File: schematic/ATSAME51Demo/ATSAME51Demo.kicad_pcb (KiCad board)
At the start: 4 copper layers, 0 parts

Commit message: First draft PCB layout
Still needs silkscreen cleanup
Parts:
- added C1: 100n, Capacitor_SMD:C_0402_1005Metric, F.Cu at (109.7, 120.5)
- added C10: 100n, Capacitor_SMD:C_0402_1005Metric, F.Cu at (90.8, 109.3)
- added C11: 4.7uF, Capacitor_SMD:C_0603_1608Metric, F.Cu at (101.7, 97.2)
- added C12: 100n, Capacitor_SMD:C_0402_1005Metric, F.Cu at (103.0, 97.5)
- added C14: 100n, Capacitor_SMD:C_0603_1608Metric, F.Cu at (64.7, 138.1)
- added C15: 10uF, Capacitor_SMD:C_0603_1608Metric, F.Cu at (64.7, 141.0)
- added C16: 100n, Capacitor_SMD:C_0603_1608Metric, F.Cu at (74.6, 73.1)
- added C17: 220n, Capacitor_SMD:C_0603_1608Metric, F.Cu at (64.1, 65.8)
- added C2: 20p, Capacitor_SMD:C_0603_1608Metric, F.Cu at (88.5, 102.9)
- added C3: 20p, Capacitor_SMD:C_0603_1608Metric, F.Cu at (88.5, 104.5)
- added C4: 100n, Capacitor_SMD:C_0402_1005Metric, F.Cu at (98.5, 118.3)
- added C5: 100n, Capacitor_SMD:C_0402_1005Metric, F.Cu at (107.8, 114.0)
- added C6: 100n, Capacitor_SMD:C_0402_1005Metric, F.Cu at (107.6, 106.0)
- added C7: 10uF, Capacitor_SMD:C_0805_2012Metric, F.Cu at (137.2, 142.0)
- added C8: 100n, Capacitor_SMD:C_0402_1005Metric, F.Cu at (100.3, 101.7)
- added C9: 22uF, Capacitor_SMD:C_0603_1608Metric, F.Cu at (138.8, 137.6)
- added D1: Red, LED_SMD:LED_0603_1608Metric, F.Cu at (127.9, 155.8)
- added D2: Red, LED_SMD:LED_0603_1608Metric, F.Cu at (56.9, 111.8)
- added D3: MBR0520LT, Diode_SMD:D_SOD-123, F.Cu at (145.3, 85.8)
- added D4: MBR0520LT, Diode_SMD:D_SOD-123, F.Cu at (57.6, 79.0)
- added D5: Yellow, LED_SMD:LED_0603_1608Metric, F.Cu at (61.4, 111.8)
- added D6: Blue, LED_SMD:LED_0603_1608Metric, F.Cu at (120.4, 75.5)
- added D7: Green, LED_SMD:LED_0603_1608Metric, F.Cu at (124.9, 75.5)
- added D8: Green, LED_SMD:LED_0603_1608Metric, F.Cu at (80.5, 70.7)
- added D9: Yellow, LED_SMD:LED_0603_1608Metric, F.Cu at (80.5, 67.0)
- added IC1: ATSAME51J20A-AU, SamacSys_Parts:QFP50P1200X1200X120-64N, F.Cu at (100.0, 110.0)
- added IC2: AZ1117IH-3.3TRG1, SamacSys_Parts:SOT230P700X180-4N, F.Cu at (144.2, 138.9)
- added IC3: MCP2221-I_SL, SamacSys_Parts:SOIC127P600X175-14N, F.Cu at (69.5, 67.1)
- added J1: Barrel_Jack_Switch, Connector_BarrelJack:BarrelJack_Wuerth_6941xx301002, F.Cu at (142.4, 145.3)
- added J10: Conn_02x06_Odd_Even, Connector_PinHeader_2.54mm:PinHeader_2x06_P2.54mm_Vertical, F.Cu at (79.5, 156.8)
- added J11: Conn_02x07_Odd_Even, Connector_PinHeader_2.54mm:PinHeader_2x07_P2.54mm_Vertical, F.Cu at (71.0, 103.0)
- added J12: Conn_01x02, Connector_PinHeader_2.54mm:PinHeader_1x02_P2.54mm_Vertical, F.Cu at (101.4, 70.3)
- added J13: Conn_01x08, Connector_PinHeader_2.54mm:PinHeader_1x08_P2.54mm_Horizontal, F.Cu at (94.0, 65.0)
- added J14: Conn_02x08_Odd_Even, Connector_PinHeader_2.54mm:PinHeader_2x08_P2.54mm_Vertical, F.Cu at (89.3, 138.0)
- added J15: Conn_02x06_Odd_Even, Connector_PinHeader_2.54mm:PinHeader_2x06_P2.54mm_Vertical, F.Cu at (132.0, 117.0)
- added J16: Conn_02x07_Odd_Even, Connector_PinHeader_2.54mm:PinHeader_2x07_P2.54mm_Vertical, F.Cu at (109.4, 80.2)
- added J2: Power, Connector_PinHeader_2.54mm:PinHeader_2x03_P2.54mm_Vertical, F.Cu at (128.3, 146.5)
- added J3: Conn_01x02, Connector_PinHeader_2.54mm:PinHeader_1x02_P2.54mm_Vertical, F.Cu at (58.1, 120.5)
- added J4: USB_B_Micro, Connector_USB:USB_Micro-B_Amphenol_10104110_Horizontal, F.Cu at (147.2, 77.2)
- added J5: USB_B_Mini, Connector_USB:USB_Mini-B_Wuerth_65100516121_Horizontal, F.Cu at (55.4, 69.5)
- added J6: Conn_01x02, Connector_PinHeader_2.54mm:PinHeader_1x02_P2.54mm_Vertical, F.Cu at (121.4, 84.4)
- added J7: Conn_02x02_Odd_Even, Connector_PinHeader_2.54mm:PinHeader_2x02_P2.54mm_Vertical, F.Cu at (129.5, 123.2)
- added J8: Conn_02x02_Odd_Even, Connector_PinHeader_2.54mm:PinHeader_2x02_P2.54mm_Vertical, F.Cu at (129.2, 135.3)
- added J9: Micro SD Card, SamacSys_Parts:MEM20750014001A, F.Cu at (65.0, 154.0)
- added L1: 470R, Inductor_SMD:L_0603_1608Metric, F.Cu at (88.2, 109.5)
- added L2: 10uH, Inductor_SMD:L_0603_1608Metric, F.Cu at (101.6, 100.3)
- added R1: 100k, Resistor_SMD:R_0603_1608Metric, F.Cu at (132.1, 63.6)
- added R10: 100k, Resistor_SMD:R_0603_1608Metric, F.Cu at (84.1, 149.9)
- added R11: 4k7, Resistor_SMD:R_0603_1608Metric, F.Cu at (128.7, 129.2)
- added R12: 100k, Resistor_SMD:R_0603_1608Metric, F.Cu at (87.5, 149.9)
- added R13: 10k, Resistor_SMD:R_0603_1608Metric, F.Cu at (90.8, 149.9)
- added R14: 4k7, Resistor_SMD:R_0603_1608Metric, F.Cu at (132.3, 129.4)
- added R15: 100k, Resistor_SMD:R_0603_1608Metric, F.Cu at (80.8, 149.9)
- added R16: 10k, Resistor_SMD:R_0603_1608Metric, F.Cu at (94.2, 149.9)
- added R17: 10k, Resistor_SMD:R_0603_1608Metric, F.Cu at (105.1, 70.0)
- added R18: 10k, Resistor_SMD:R_0603_1608Metric, F.Cu at (78.7, 63.5)
- added R19: 220R, Resistor_SMD:R_0603_1608Metric, F.Cu at (77.4, 70.7)
- added R2: 220R, Resistor_SMD:R_0603_1608Metric, F.Cu at (132.3, 155.8)
- added R20: 220R, Resistor_SMD:R_0603_1608Metric, F.Cu at (77.4, 67.0)
- added R5: 220R, Resistor_SMD:R_0603_1608Metric, F.Cu at (56.9, 115.4)
- added R6: 220R, Resistor_SMD:R_0603_1608Metric, F.Cu at (61.4, 115.4)
- added R7: 220R, Resistor_SMD:R_0603_1608Metric, F.Cu at (120.4, 79.6)
- added R8: 220R, Resistor_SMD:R_0603_1608Metric, F.Cu at (124.9, 79.6)
- added R9: 100k, Resistor_SMD:R_0603_1608Metric, F.Cu at (77.4, 149.9)
- added SW1: SW_MEC_5E, SamacSys_Parts:PTS647SK38SMTR2LFS, F.Cu at (125.0, 65.4)
- added SW2: SW_MEC_5E, SamacSys_Parts:FSM16JH, F.Cu at (60.5, 91.8)
- added SW3: SW_MEC_5E, SamacSys_Parts:FSM16JH, F.Cu at (80.8, 91.8)
- added X1: 12 MHz, SamacSys_Parts:ASTMUPCE3312000MHZLJET, F.Cu at (107.1, 120.5)
- added X2: 32.768 kHz 12.5 pF, SamacSys_Parts:CM9VT1A, F.Cu at (91.1, 103.7)
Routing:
- net VIN: track 0.00 -> 170.9 mm, vias 0 -> 2
- net SD_CD: track 0.00 -> 94.4 mm, vias 0 -> 1
- net GND: track 0.00 -> 88.5 mm, vias 0 -> 29
- net TX0: track 0.00 -> 78.5 mm, vias 0 -> 1
- net RX0: track 0.00 -> 78.0 mm, vias 0 -> 2
- net SD_CLK: track 0.00 -> 71.3 mm, vias 0 -> 1
- net SD_DAT0: track 0.00 -> 71.0 mm, vias 0 -> 2
- net SD_DAT1: track 0.00 -> 69.6 mm, vias 0 -> 2
- net SD_CMD: track 0.00 -> 66.0 mm, vias 0 -> 2
- net SD_DAT3: track 0.00 -> 64.3 mm, vias 0 -> 2
- net RESETN: track 0.00 -> 64.2 mm, vias 0 -> 2
- net SD_DAT2: track 0.00 -> 61.0 mm, vias 0 -> 2
- net VCC3V3: track 0.00 -> 57.0 mm, vias 0 -> 15
- net PB04: track 0.00 -> 54.0 mm
- net PB31: track 0.00 -> 53.6 mm, vias 0 -> 1
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- added copper zone on In1.Cu, net GND
- added copper zone on In2.Cu, net VCC3V3
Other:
- board outline added: 100 x 100 mm

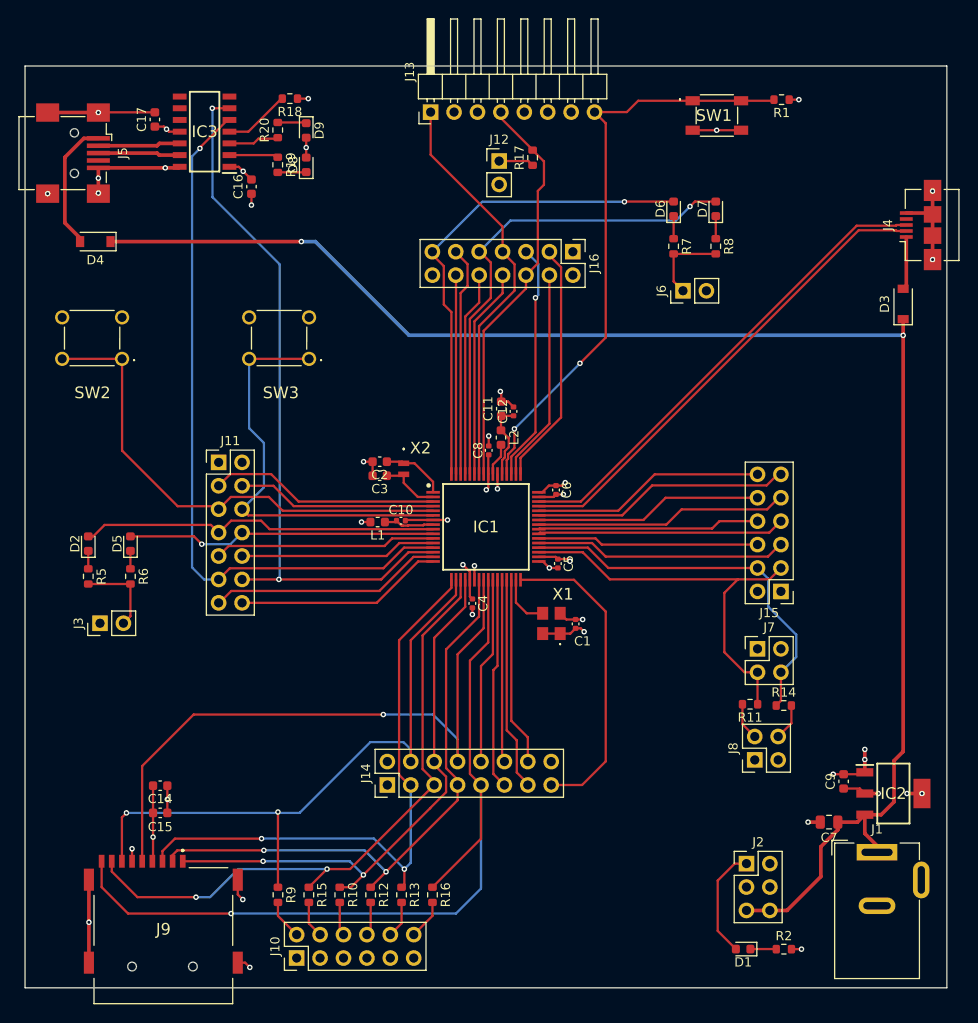
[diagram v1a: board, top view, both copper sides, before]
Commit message: Front silkscreen done
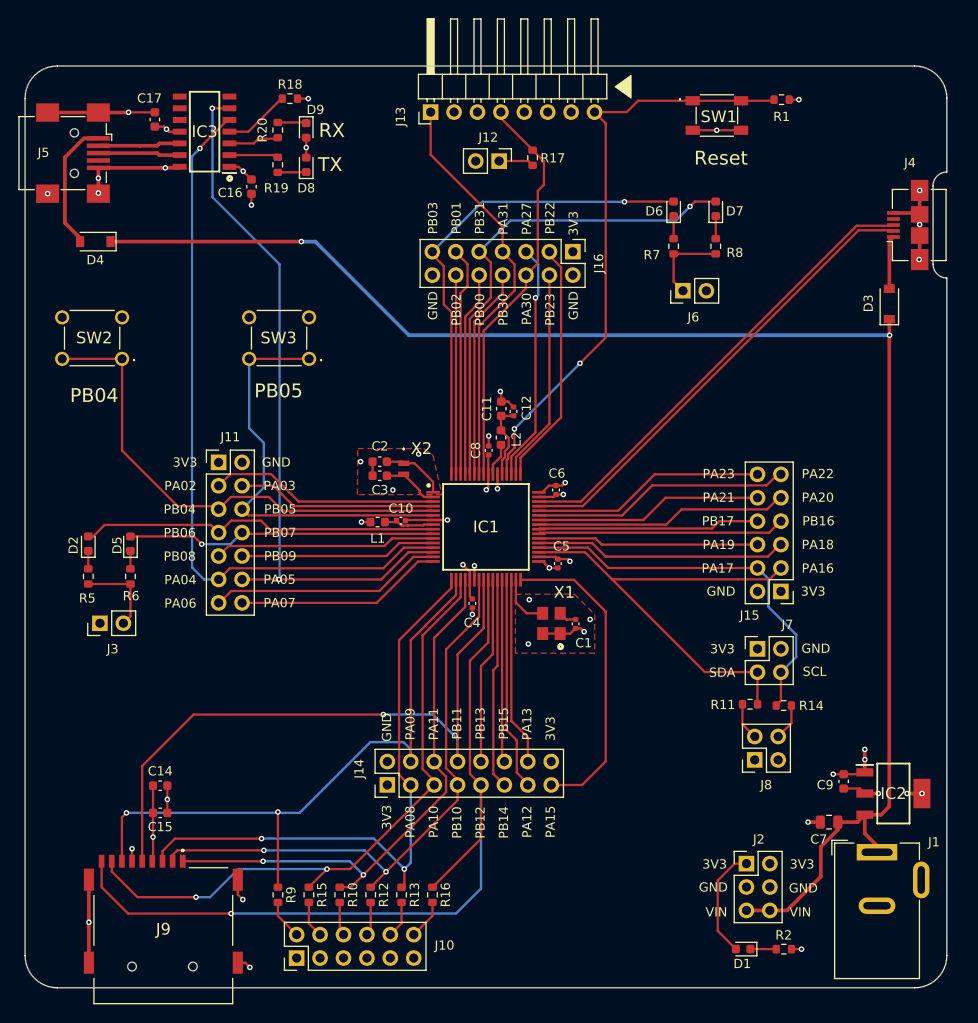
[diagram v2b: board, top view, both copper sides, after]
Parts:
- moved D3 1.50 mm to (143.8, 85.8)
- moved J4 1.40 mm to (145.8, 77.2)
- turned J12 to 270 degrees
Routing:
- net SERCOM1_PAD0: track 44.5 -> 51.4 mm
- net VIN: track 170.9 -> 168.8 mm
- net GND: track 88.5 -> 86.7 mm, vias 29 -> 34
- net D-: track 52.3 -> 50.9 mm
- net D+: track 52.3 -> 50.9 mm
- net Net-(D3-Pad2): track 5.76 -> 6.28 mm
- added copper zone on F.Cu, net GND
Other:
- outline, holes or cut-outs redrawn
- board text added: "3V3"
- board text added: "GND"
- board text added: "PA02"
- board text added: "PA03"
- board text added: "PA04"
- board text added: "PA05"
- board text added: "PA06"
- board text added: "PA07"
- board text added: "PA08"
- board text added: "PA09"
- board text added: "PA10"
- board text added: "PA11"
- board text added: "PA12"
- board text added: "PA13"
- board text added: "PA15"
- board text added: "PA16"
- board text added: "PA17"
- board text added: "PA18"
- board text added: "PA19"
- board text added: "PA20"
- board text added: "PA21"
- board text added: "PA22"
- board text added: "PA23"
- board text added: "PA27"
- board text added: "PA30"
- board text added: "PA31"
- board text added: "PB00"
- board text added: "PB01"
- board text added: "PB02"
- board text added: "PB03"
- board text added: "PB04"
- board text added: "PB05"
- board text added: "PB06"
- board text added: "PB07"
- board text added: "PB08"
- board text added: "PB09"
- board text added: "PB10"
- board text added: "PB11"
- board text added: "PB12"
- board text added: "PB13"
- board text added: "PB14"
- board text added: "PB15"
- board text added: "PB16"
- board text added: "PB17"
- board text added: "PB22"
- board text added: "PB23"
- board text added: "PB30"
- board text added: "PB31"
- board text added: "RX"
- board text added: "Reset"
- board text added: "SCL"
- board text added: "SDA"
- board text added: "TX"
- board text added: "VIN"

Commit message: Moved SD card back from edge
Rearranged some connections to improve routing
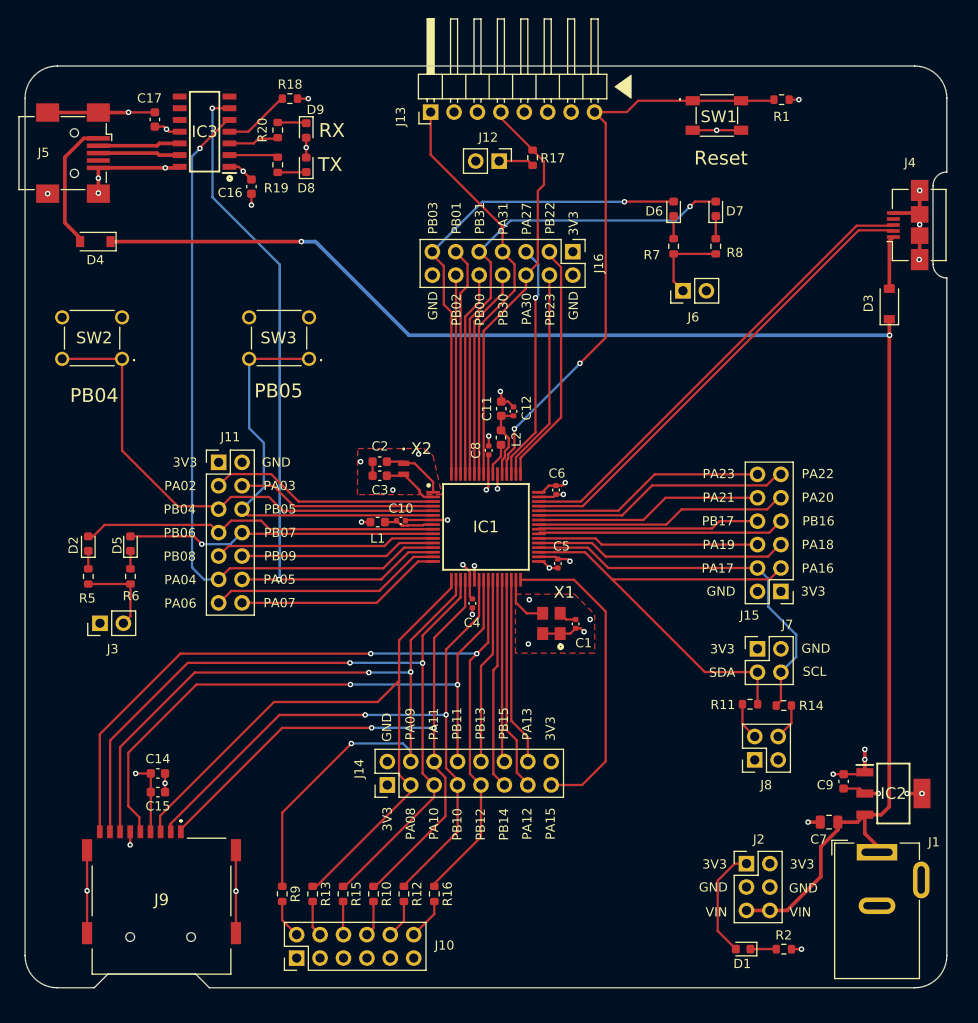
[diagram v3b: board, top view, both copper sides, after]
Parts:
- moved R13 9.64 mm to (81.2, 149.8)
- moved R15 3.71 mm to (84.5, 149.8)
- moved R10 3.66 mm to (87.8, 149.8)
- moved R12 3.61 mm to (91.1, 149.8)
- moved J9 3.21 mm to (64.8, 150.8)
- moved C15 2.26 mm to (64.4, 138.8)
- moved C14 1.35 mm to (64.4, 136.8)
- moved R9 0.48 mm to (77.9, 149.8)
- moved R16 0.22 mm to (94.4, 149.8)
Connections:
- R10 pad 2: Net-(J10-Pad6) -> Net-(J10-Pad8)
- R12 pad 2: Net-(J10-Pad8) -> Net-(J10-Pad10)
- R13 pad 2: Net-(J10-Pad10) -> Net-(J10-Pad4)
- R15 pad 2: Net-(J10-Pad4) -> Net-(J10-Pad6)
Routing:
- net SD_DAT0: track 71.0 -> 92.3 mm, vias 2 -> 3
- net SD_DAT1: track 69.6 -> 87.0 mm
- net SD_DAT2: track 61.0 -> 70.9 mm
- net SD_DAT3: track 64.3 -> 73.3 mm
- net SD_CMD: track 66.0 -> 75.0 mm, vias 2 -> 0
- net GND: track 86.7 -> 91.0 mm, vias 34 -> 33
- net SD_CD: track 94.4 -> 91.8 mm, vias 1 -> 2
- net SD_CLK: track 71.3 -> 68.8 mm, vias 1 -> 2
- net Net-(J10-Pad8): track 3.66 -> 4.46 mm
- net Net-(J10-Pad6): track 3.66 -> 4.19 mm
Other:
- outline, holes or cut-outs redrawn
- board text added: "ATSAME51J20 Demo Board V1.0"
- board text added: "JLCJLCJLCJLC"
- board text added: "Jumpers J3, J6 = LED enable J8 = I2C pull-ups J10 = SD card pull-ups J12 = SWCLK pull-up"
- board text added: "QES 2021"

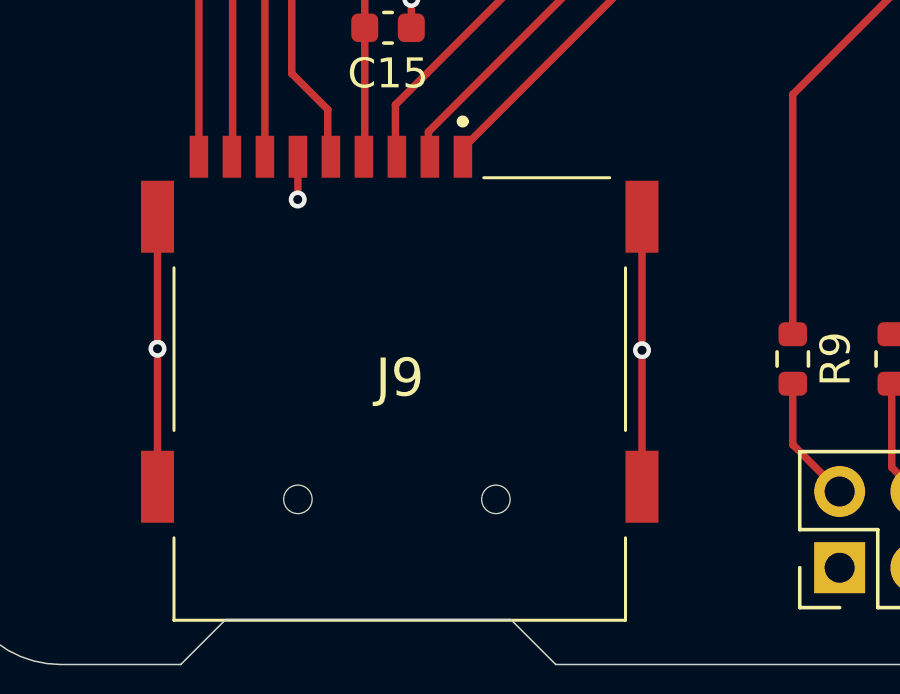
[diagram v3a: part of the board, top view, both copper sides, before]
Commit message: Adjusted sd card footprint
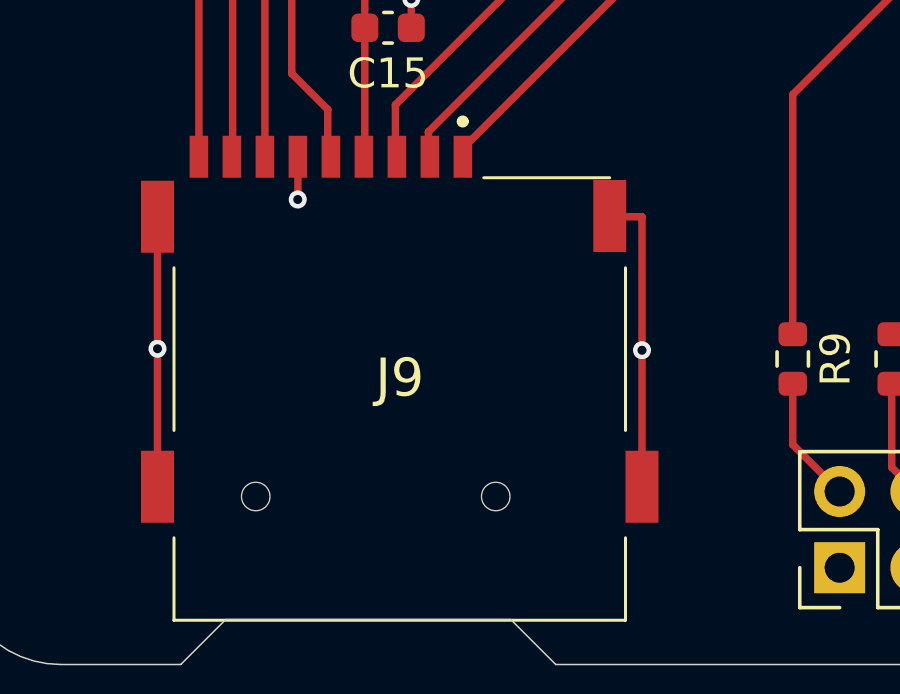
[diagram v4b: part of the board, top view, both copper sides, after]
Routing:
- net GND: track 91.0 -> 92.0 mm
